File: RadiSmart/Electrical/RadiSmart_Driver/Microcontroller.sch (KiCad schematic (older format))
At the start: 12 parts, among them P1 Pikit header, U7 PIC18F26K42, Y1 Crystal, Y2 Crystal

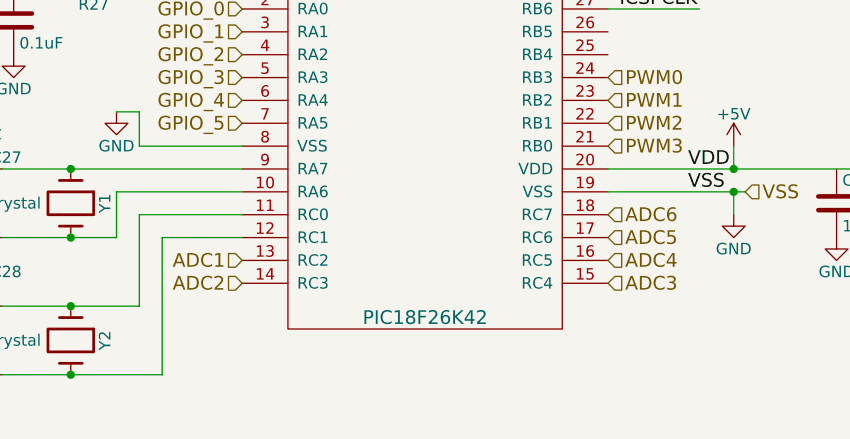
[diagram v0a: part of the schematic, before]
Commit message: added more datasheets for interesting chips, temperature sensing and real-time clock
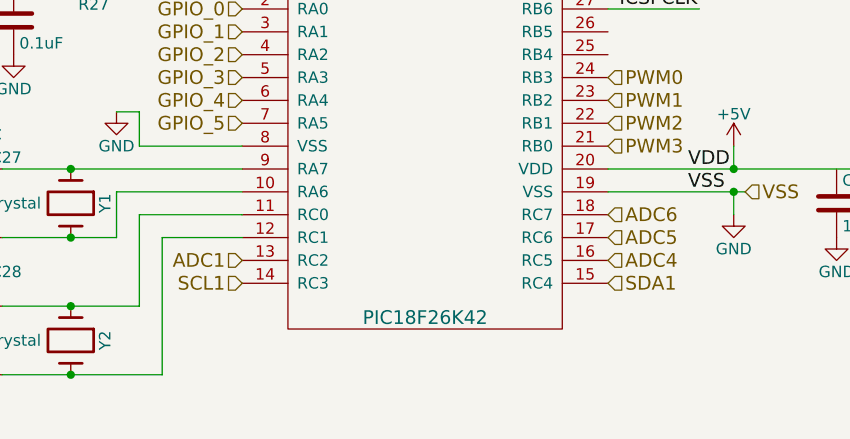
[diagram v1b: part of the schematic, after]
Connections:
- net labels added: SCL1, SDA1
- net labels removed: ADC2, ADC3
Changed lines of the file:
@@
 LIBS:contrib
 LIBS:valves
-LIBS:MRV_ICs
 LIBS:RadiSmart_Driver-cache
 EELAYER 25 0
@@
 ADC1
 Text HLabel 4700 4250 0    60   Input ~ 0
-ADC2
+SCL1
 Text HLabel 6300 4250 2    60   Input ~ 0
-ADC3
+SDA1
 Text HLabel 6300 4150 2    60   Input ~ 0
 ADC4

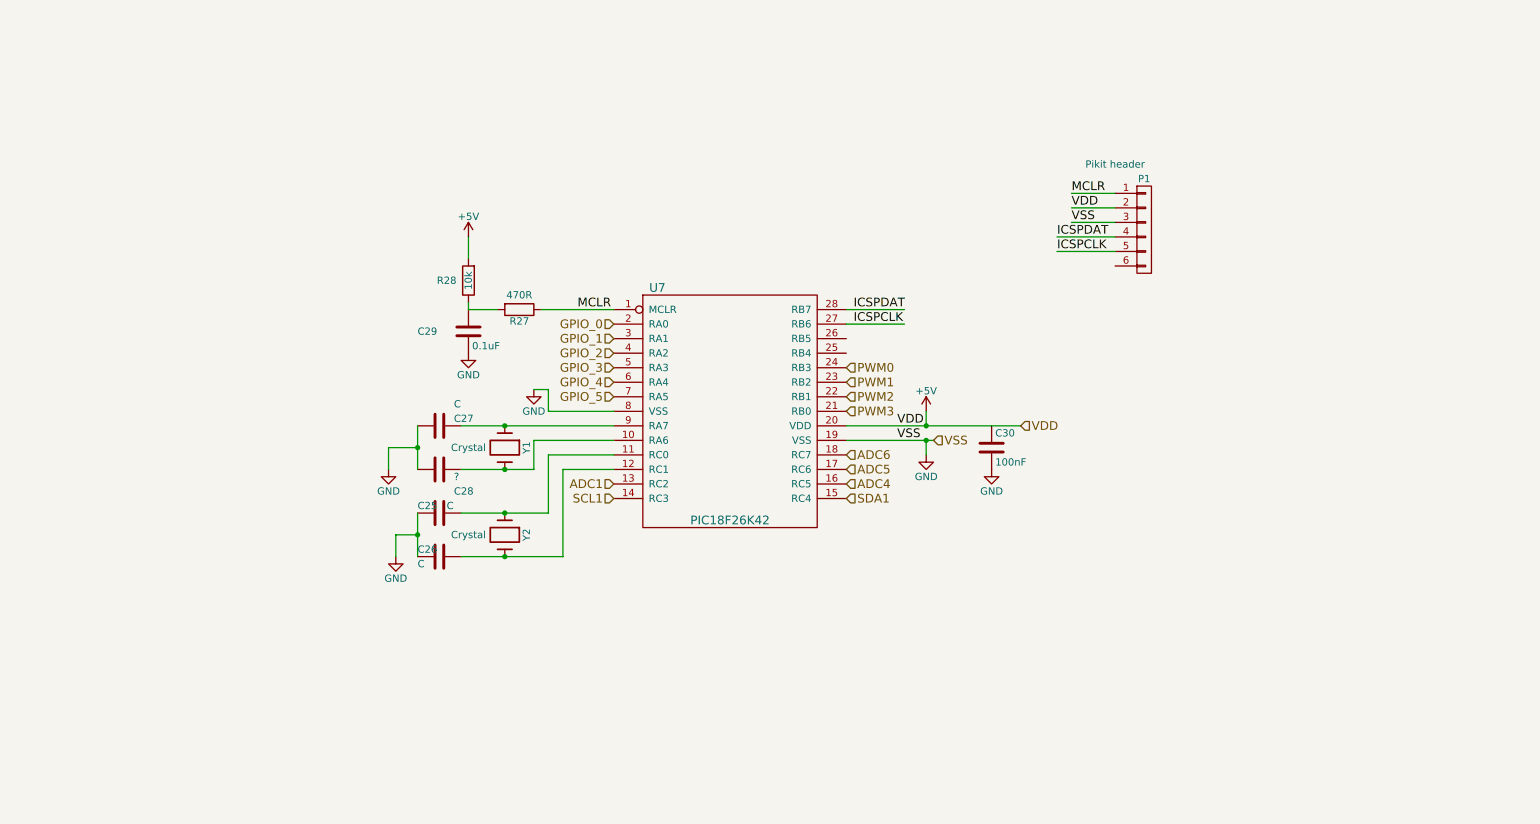
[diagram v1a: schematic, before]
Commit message: switching from 12V to 24V to support more LEDs per channel
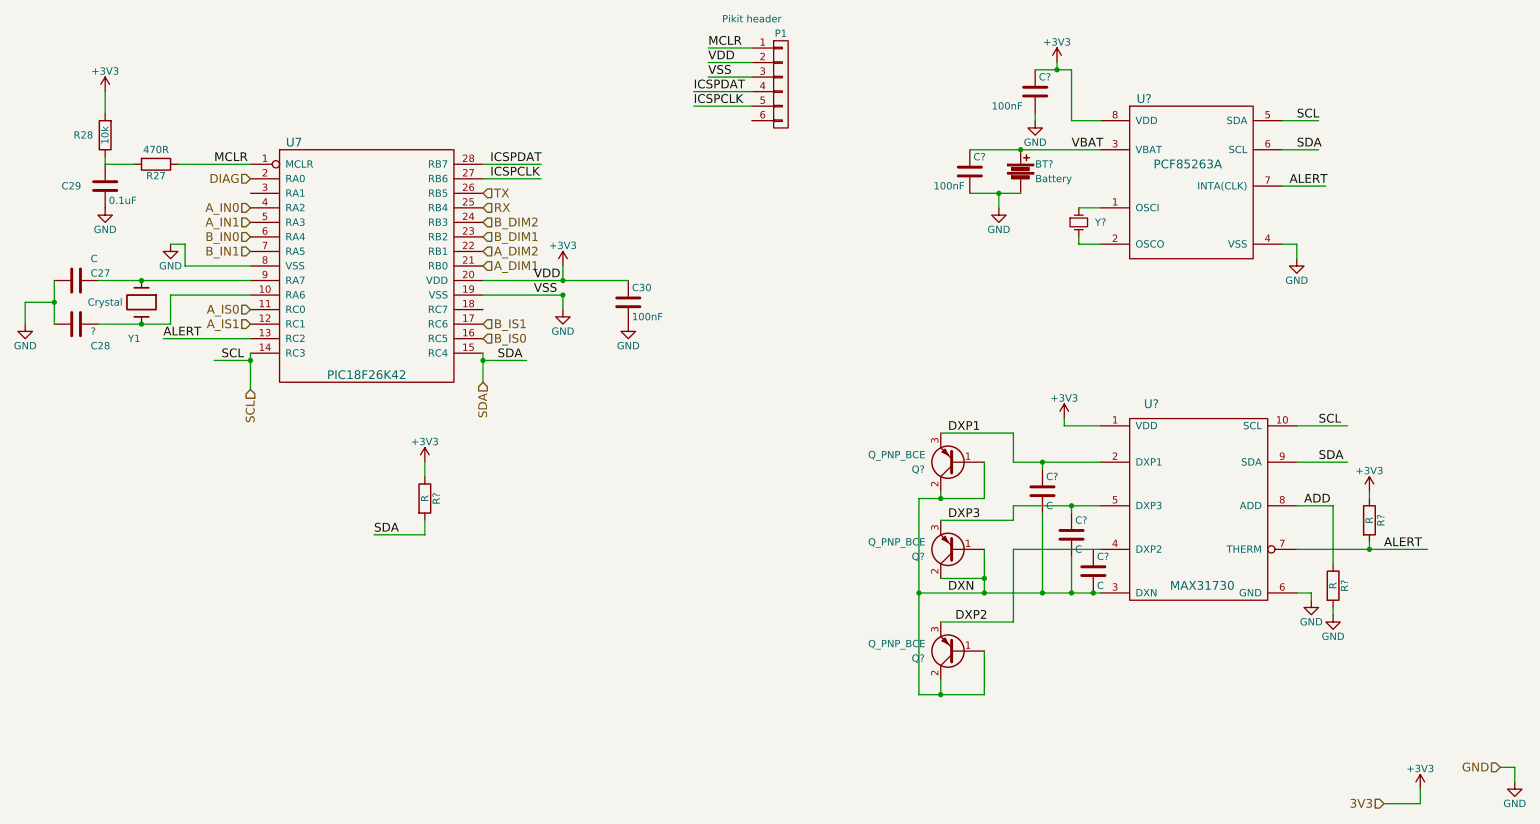
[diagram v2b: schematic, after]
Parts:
- removed C25, C26: C, Capacitors_SMD:C_0805, symbol C
- removed Y2: Crystal, Crystals:Crystal_Watch, symbol Crystal
- added BT?: Battery, symbol Battery
- added C? (x3): C, symbol C
- added C? (x2): 100nF, symbol C
- added Q? (x3): Q_PNP_BCE, symbol Q_PNP_BCE
- added R? (x3): R, symbol R
- added U?: MAX31730, symbol MAX31730
- added U?: PCF85263A, symbol PCF85263A
- added Y?: Crystal_Small, symbol Crystal_Small
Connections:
- net labels added: +3V3, 3V3, ADD, ALERT, A_DIM1, A_DIM2, A_IN0, A_IN1, A_IS0, A_IS1, B_DIM1, B_DIM2, B_IN0, B_IN1, B_IS0, B_IS1, DIAG, DXN, DXP1, DXP2, DXP3, RX, SCL, SDA, TX, VBAT
- net labels removed: +5V, ADC1, ADC4, ADC5, ADC6, GPIO_0, GPIO_1, GPIO_2, GPIO_3, GPIO_4, GPIO_5, PWM0, PWM1, PWM2, PWM3, SCL1, SDA1
- wire segments 34 -> 88
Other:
- moved on the sheet: C27, C28, C29, C30, P1, R27, R28, U7, Y1
